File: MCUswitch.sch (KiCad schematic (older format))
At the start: 4 parts, among them Q4 TSM2314

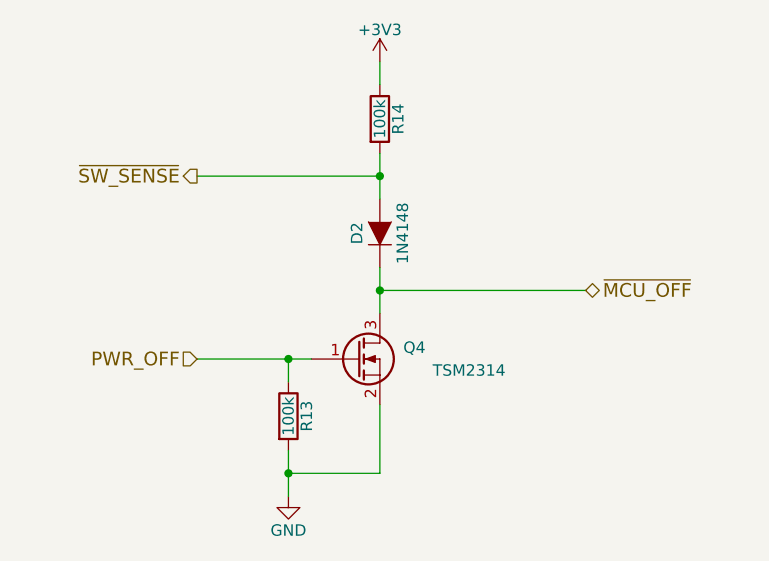
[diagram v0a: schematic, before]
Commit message: Finished adding full part descriptions
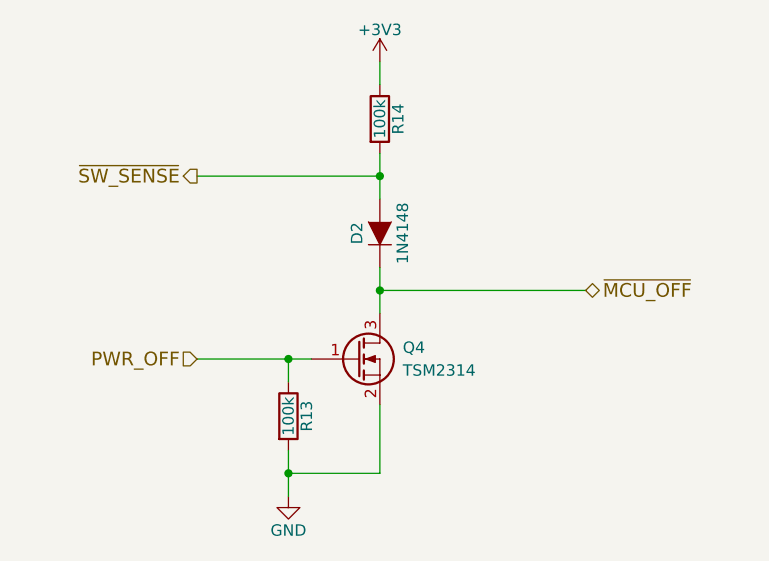
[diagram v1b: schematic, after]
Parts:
- D2: Alt. Order Code (none) -> 512-1N4148WS; Alt. Supplier (none) -> Mouser; Manufacturer (none) -> Multicomp; Note (none) -> Small signal SOD-323 diode; Order Code (none) -> 1466524; Package (none) -> SOD-323; Part Number (none) -> 1N4148WS; Supplier (none) -> Farnell
- Q4: Alt. Order Code (none) -> 781-SI2314EDS-E3; Alt. Supplier (none) -> Mouser; Manufacturer (none) -> Taiwan Semiconductor; Note (none) -> N-channel SOT-23 MOSFET; Order Code (none) -> 1864589; Package (none) -> SOT-23; Part Number (none) -> TSM2314CX
- R13, R14: Alt. Order Code (none) -> 71-CRCW0805-100K-E3; Alt. Supplier (none) -> Mouser; Manufacturer (none) -> Multicomp; Note (none) -> 100kΩ/1% 0805 resistor; Order Code (none) -> 2447551; Package (none) -> 0805; Part Number (none) -> MCWR08X1003FTL; Supplier (none) -> Farnell
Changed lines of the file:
@@
 U 1 1 56CEA3CE
 P 5000 3000
-F 0 "Q4" H 5300 3050 50  0000 R CNN
-F 1 "TSM2314" H 5650 2950 50  0000 R CNN
+F 0 "Q4" H 5200 3050 50  0000 L CNN
+F 1 "TSM2314" H 5200 2950 50  0000 L CNN
 F 2 "TO_SOT_Packages_SMD:SOT-23" H 5200 3100 50  0001 C CNN
 F 3 "" H 5000 3000 50  0000 C CNN
-F 4 "Farnell" H 5000 3000 60  0001 C CNN "Supplier"
+F 4 "TSM2314CX" H 5000 3000 60  0001 C CNN "Part Number"
+F 5 "Taiwan Semiconductor" H 5000 3000 60  0001 C CNN "Manufacturer"
+F 6 "SOT-23" H 5000 3000 60  0001 C CNN "Package"
+F 7 "Farnell" H 5000 3000 60  0001 C CNN "Supplier"
+F 8 "1864589" H 5000 3000 60  0001 C CNN "Order Code"
+F 9 "Mouser" H 5000 3000 60  0001 C CNN "Alt. Supplier"
+F 10 "781-SI2314EDS-E3" H 5000 3000 60  0001 C CNN "Alt. Order Code"
+F 11 "N-channel SOT-23 MOSFET" H 5000 3000 60  0001 C CNN "Note"
 	1    5000 3000
 	1    0    0    -1
@@
 F 2 "Resistors_SMD:R_0805" V 4630 3250 50  0001 C CNN
 F 3 "" H 4700 3250 50  0000 C CNN
+F 4 "MCWR08X1003FTL" H 4700 3250 60  0001 C CNN "Part Number"
+F 5 "Multicomp" H 4700 3250 60  0001 C CNN "Manufacturer"
+F 6 "0805" H 4700 3250 60  0001 C CNN "Package"
+F 7 "Farnell" H 4700 3250 60  0001 C CNN "Supplier"
+F 8 "2447551" H 4700 3250 60  0001 C CNN "Order Code"
+F 9 "Mouser" H 4700 3250 60  0001 C CNN "Alt. Supplier"
+F 10 "71-CRCW0805-100K-E3" H 4700 3250 60  0001 C CNN "Alt. Order Code"
+F 11 "100kΩ/1% 0805 resistor" H 4700 3250 60  0001 C CNN "Note"
 	1    4700 3250
 	1    0    0    -1
@@
 F 2 "Diodes_SMD:SOD-323" H 5100 2450 50  0001 C CNN
 F 3 "" H 5100 2450 50  0000 C CNN
+F 4 "1N4148WS" H 5100 2450 60  0001 C CNN "Part Number"
+F 5 "Multicomp" H 5100 2450 60  0001 C CNN "Manufacturer"
+F 6 "SOD-323" H 5100 2450 60  0001 C CNN "Package"
+F 7 "Farnell" H 5100 2450 60  0001 C CNN "Supplier"
+F 8 "1466524" H 5100 2450 60  0001 C CNN "Order Code"
+F 9 "Mouser" H 5100 2450 60  0001 C CNN "Alt. Supplier"
+F 10 "512-1N4148WS" H 5100 2450 60  0001 C CNN "Alt. Order Code"
+F 11 "Small signal SOD-323 diode" H 5100 2450 60  0001 C CNN "Note"
 	1    5100 2450
 	0    -1   -1   0
@@
 F 2 "Resistors_SMD:R_0805" V 5030 1950 50  0001 C CNN
 F 3 "" H 5100 1950 50  0000 C CNN
+F 4 "MCWR08X1003FTL" H 5100 1950 60  0001 C CNN "Part Number"
+F 5 "Multicomp" H 5100 1950 60  0001 C CNN "Manufacturer"
+F 6 "0805" H 5100 1950 60  0001 C CNN "Package"
+F 7 "Farnell" H 5100 1950 60  0001 C CNN "Supplier"
+F 8 "2447551" H 5100 1950 60  0001 C CNN "Order Code"
+F 9 "Mouser" H 5100 1950 60  0001 C CNN "Alt. Supplier"
+F 10 "71-CRCW0805-100K-E3" H 5100 1950 60  0001 C CNN "Alt. Order Code"
+F 11 "100kΩ/1% 0805 resistor" H 5100 1950 60  0001 C CNN "Note"
 	1    5100 1950
 	1    0    0    -1

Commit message: Changed SHIELD1 to A1, changed SOD-323 footprint for easier soldering
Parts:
- D2: footprint Diodes_SMD:SOD-323 -> jakub:SOD-323
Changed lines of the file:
@@
 F 0 "D2" H 5100 2550 50  0000 C CNN
 F 1 "1N4148" H 5100 2350 50  0000 C CNN
-F 2 "Diodes_SMD:SOD-323" H 5100 2450 50  0001 C CNN
+F 2 "jakub:SOD-323" H 5100 2450 50  0001 C CNN
 F 3 "" H 5100 2450 50  0000 C CNN
 F 4 "1N4148WS" H 5100 2450 60  0001 C CNN "Part Number"
